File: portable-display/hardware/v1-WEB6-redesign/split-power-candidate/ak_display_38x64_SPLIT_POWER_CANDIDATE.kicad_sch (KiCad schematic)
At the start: 0 parts

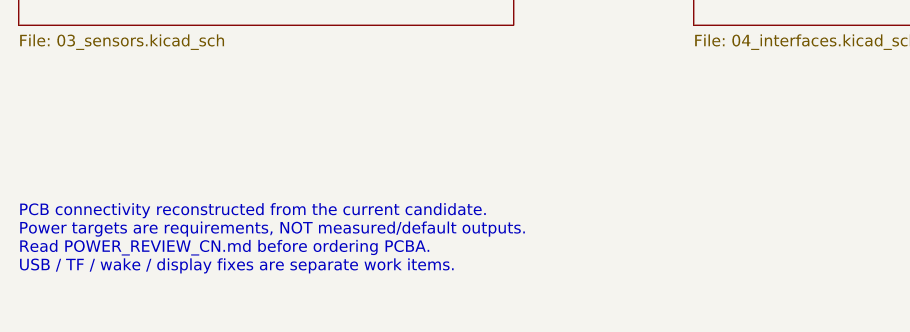
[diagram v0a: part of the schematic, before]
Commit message: fix: resolve screen RESET/TE level matching
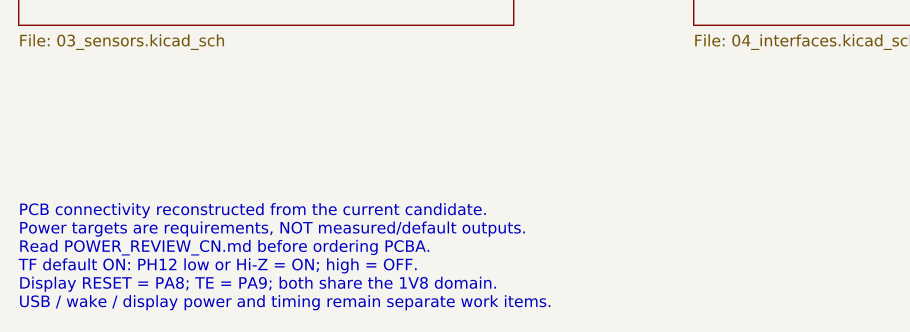
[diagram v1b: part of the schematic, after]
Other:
- note added: "PCB connectivity reconstructed from the current candidate. Power targets are requirements, NOT measured/default outputs. Read POWER_REVIEW_CN.md before ordering PCBA. TF default ON: PH12 low or Hi-Z = ON; high = OFF. Display RESET = PA8; TE = PA9; both share the 1V8 domain. USB / wake / display power and timing remain separate work items."
- note removed: "PCB connectivity reconstructed from the current candidate. Power targets are requirements, NOT measured/default outputs. Read POWER_REVIEW_CN.md before ordering PCBA. USB / TF / wake / display fixes are separate work items."
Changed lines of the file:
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@@
 	(title_block
 		(title "38x64 split-power candidate - connectivity schematic")
-		(date "2026-09-20")
-		(rev "PWR-REVIEW1")
+		(date "2026-09-24")
+		(rev "LCD-IO1")
 		(company "Sameat")
 		(comment 1 "Power configuration incomplete: C3036461 factory profile not confirmed")
@@
 		)
 	)
-	(text "PCB connectivity reconstructed from the current candidate.\nPower targets are requirements, NOT measured/default outputs.\nRead POWER_REVIEW_CN.md before ordering PCBA.\nUSB / TF / wake / display fixes are separate work items."
+	(text "PCB connectivity reconstructed from the current candidate.\nPower targets are requirements, NOT measured/default outputs.\nRead POWER_REVIEW_CN.md before ordering PCBA.\nTF default ON: PH12 low or Hi-Z = ON; high = OFF.\nDisplay RESET = PA8; TE = PA9; both share the 1V8 domain.\nUSB / wake / display power and timing remain separate work items."
 		(exclude_from_sim no)
 		(at 25 150 0)

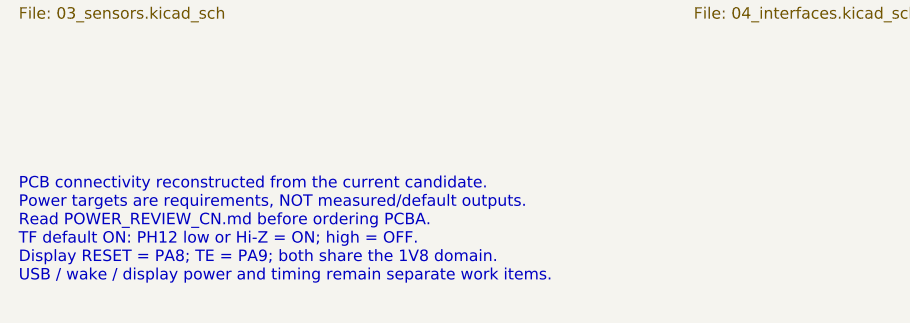
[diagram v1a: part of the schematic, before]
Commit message: fix(hardware): extend automatic wake pulse to nominal 3 seconds
Use a 910k resistor and 3.3uF 0805 timing capacitor, bind JLCPCB parts, and reroute the timing nets. Synchronize schematics, local footprint and independent component requirements. Physical timing and retrigger behavior remain subject to validation.
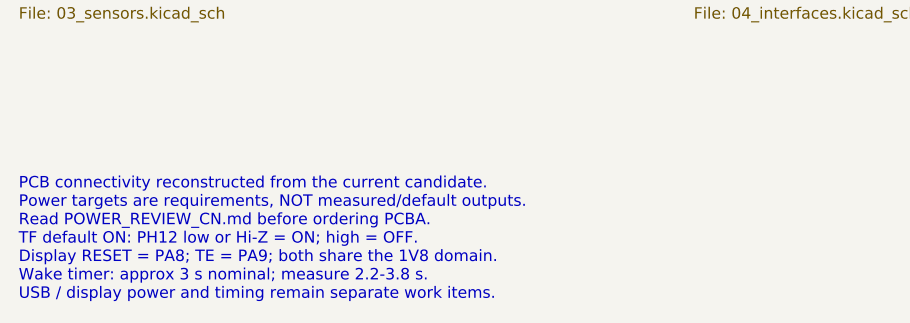
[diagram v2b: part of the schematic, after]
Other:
- note added: "PCB connectivity reconstructed from the current candidate. Power targets are requirements, NOT measured/default outputs. Read POWER_REVIEW_CN.md before ordering PCBA. TF default ON: PH12 low or Hi-Z = ON; high = OFF. Display RESET = PA8; TE = PA9; both share the 1V8 domain. Wake timer: approx 3 s nominal; measure 2.2-3.8 s. USB / display power and timing remain separate work items."
- note removed: "PCB connectivity reconstructed from the current candidate. Power targets are requirements, NOT measured/default outputs. Read POWER_REVIEW_CN.md before ordering PCBA. TF default ON: PH12 low or Hi-Z = ON; high = OFF. Display RESET = PA8; TE = PA9; both share the 1V8 domain. USB / wake / display power and timing remain separate work items."
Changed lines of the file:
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@@
 	(title_block
 		(title "38x64 split-power candidate - connectivity schematic")
-		(date "2026-09-24")
-		(rev "LCD-IO1")
+		(date "2026-10-01")
+		(rev "WAKE1")
 		(company "Sameat")
 		(comment 1 "Power configuration incomplete: C3036461 factory profile not confirmed")
@@
 		)
 	)
-	(text "PCB connectivity reconstructed from the current candidate.\nPower targets are requirements, NOT measured/default outputs.\nRead POWER_REVIEW_CN.md before ordering PCBA.\nTF default ON: PH12 low or Hi-Z = ON; high = OFF.\nDisplay RESET = PA8; TE = PA9; both share the 1V8 domain.\nUSB / wake / display power and timing remain separate work items."
+	(text "PCB connectivity reconstructed from the current candidate.\nPower targets are requirements, NOT measured/default outputs.\nRead POWER_REVIEW_CN.md before ordering PCBA.\nTF default ON: PH12 low or Hi-Z = ON; high = OFF.\nDisplay RESET = PA8; TE = PA9; both share the 1V8 domain.\nWake timer: approx 3 s nominal; measure 2.2-3.8 s.\nUSB / display power and timing remain separate work items."
 		(exclude_from_sim no)
 		(at 25 150 0)

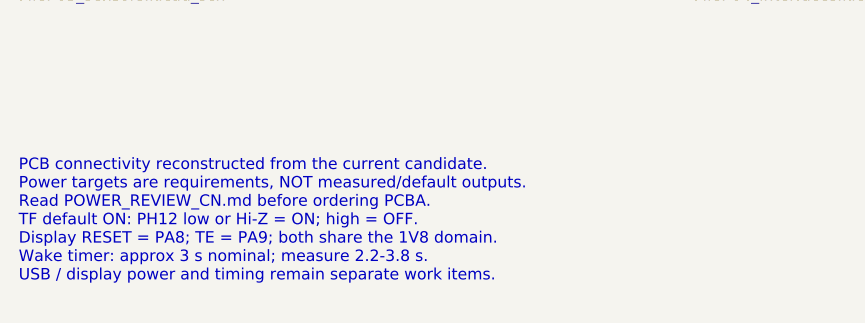
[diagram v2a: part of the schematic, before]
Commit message: fix: repair USB routing by swapping DP/DM pins on U9 and updating layout files
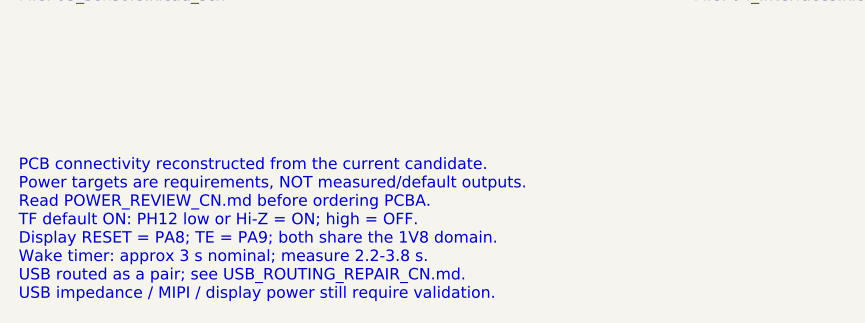
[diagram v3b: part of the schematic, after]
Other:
- note added: "PCB connectivity reconstructed from the current candidate. Power targets are requirements, NOT measured/default outputs. Read POWER_REVIEW_CN.md before ordering PCBA. TF default ON: PH12 low or Hi-Z = ON; high = OFF. Display RESET = PA8; TE = PA9; both share the 1V8 domain. Wake timer: approx 3 s nominal; measure 2.2-3.8 s. USB routed as a pair; see USB_ROUTING_REPAIR_CN.md. USB impedance / MIPI 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"
- note removed: "PCB connectivity reconstructed from the current candidate. Power targets are requirements, NOT measured/default outputs. Read POWER_REVIEW_CN.md before ordering PCBA. TF default ON: PH12 low or Hi-Z = ON; high = OFF. Display RESET = PA8; TE = PA9; both share the 1V8 domain. Wake timer: approx 3 s nominal; measure 2.2-3.8 s. USB / display power and timing remain separate work items."
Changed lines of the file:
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@@
 	(title_block
 		(title "38x64 split-power candidate - connectivity schematic")
-		(date "2026-10-01")
-		(rev "WAKE1")
+		(date "2026-10-02")
+		(rev "USB1")
 		(company "Sameat")
 		(comment 1 "Power configuration incomplete: C3036461 factory profile not confirmed")
@@
 		)
 	)
-	(text "PCB connectivity reconstructed from the current candidate.\nPower targets are requirements, NOT measured/default outputs.\nRead POWER_REVIEW_CN.md before ordering PCBA.\nTF default ON: PH12 low or Hi-Z = ON; high = OFF.\nDisplay RESET = PA8; TE = PA9; both share the 1V8 domain.\nWake timer: approx 3 s nominal; measure 2.2-3.8 s.\nUSB / display power and timing remain separate work items."
+	(text "PCB connectivity reconstructed from the current candidate.\nPower targets are requirements, NOT measured/default outputs.\nRead POWER_REVIEW_CN.md before ordering PCBA.\nTF default ON: PH12 low or Hi-Z = ON; high = OFF.\nDisplay RESET = PA8; TE = PA9; both share the 1V8 domain.\nWake timer: approx 3 s nominal; measure 2.2-3.8 s.\nUSB routed as a pair; see USB_ROUTING_REPAIR_CN.md.\nUSB impedance / MIPI / display power still require validation."
 		(exclude_from_sim no)
 		(at 25 150 0)
